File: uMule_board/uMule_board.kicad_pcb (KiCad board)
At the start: 2 copper layers, 140 x 140 mm, 212 parts, among them J1 12V IN, J10 Conn_02x04_Odd_Even, J11 Conn_01x04, J12 Conn_01x04, J13 Conn_01x04, J2 Dynamixel, J21 OUT3, J23 I2C, J26 SPI_IMU, J3 OUT3, J4 Conn_ST_STDC14, J5 OUT3, J6 OUT3, J7 ESP32_UART, J8 Li-Dar_UART, J9 Conn_02x04_Odd_Even, P1 BPV10NF, P10 BPV10NF, P11 BPV10NF, P12 BPV10NF, P13 BPV10NF, P14 BPV10NF, P15 BPV10NF, P16 BPV10NF, P2 BPV10NF, P3 BPV10NF, P4 BPV10NF, P5 BPV10NF, P6 BPV10NF, P7 BPV10NF, P8 BPV10NF, P9 BPV10NF, Q1 AON6407, Q2 AON6407, Q3 AON6407, Q4 AON6407, Q5 AON6407, SW1 DBG_BUTT, SW2 RST, U1 TPS62933DRLR, U10 OPA397DBVR, U11 OPA397DBVR, U12 OPA397DBVR, U13 OPA397DBVR, U14 OPA397DBVR, U15 OPA397DBVR, U16 OPA397DBVR, U17 OPA397DBVR, U18 OPA397DBVR, U19 OPA397DBVR, U2 TLV761, U20 OPA397DBVR, U21 OPA397DBVR, U22 OPA397DBVR, U23 SP3485CN, U24 EL3H7(B)(TA)-G, U25 EL3H7(B)(TA)-G, U26 EL3H7(B)(TA)-G, U3 INA219AxD, U4 EL3H7(B)(TA)-G, U5 STM32F103RCTx, U6 FM24C64B, U7 OPA397DBVR, U8 OPA397DBVR, U9 OPA397DBVR, Y1 8MHz

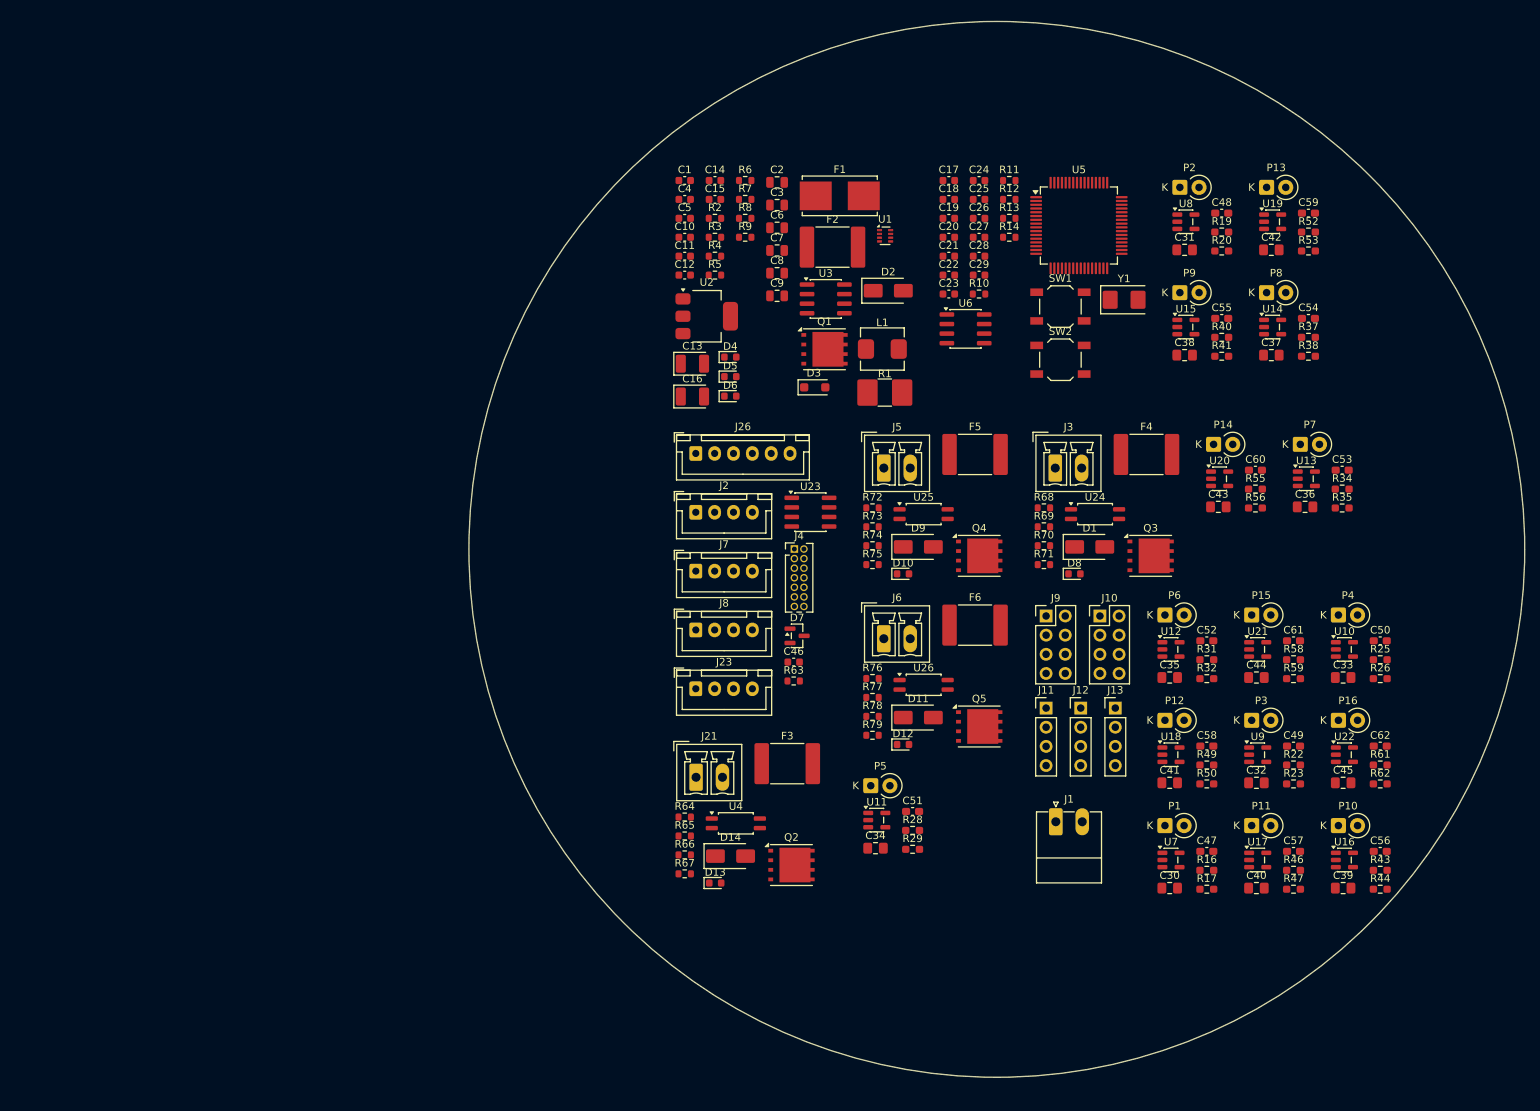
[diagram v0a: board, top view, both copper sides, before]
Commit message: Started working on PCB. Ditched high power outputs. Focusing on photodiodes. One commit closer to order
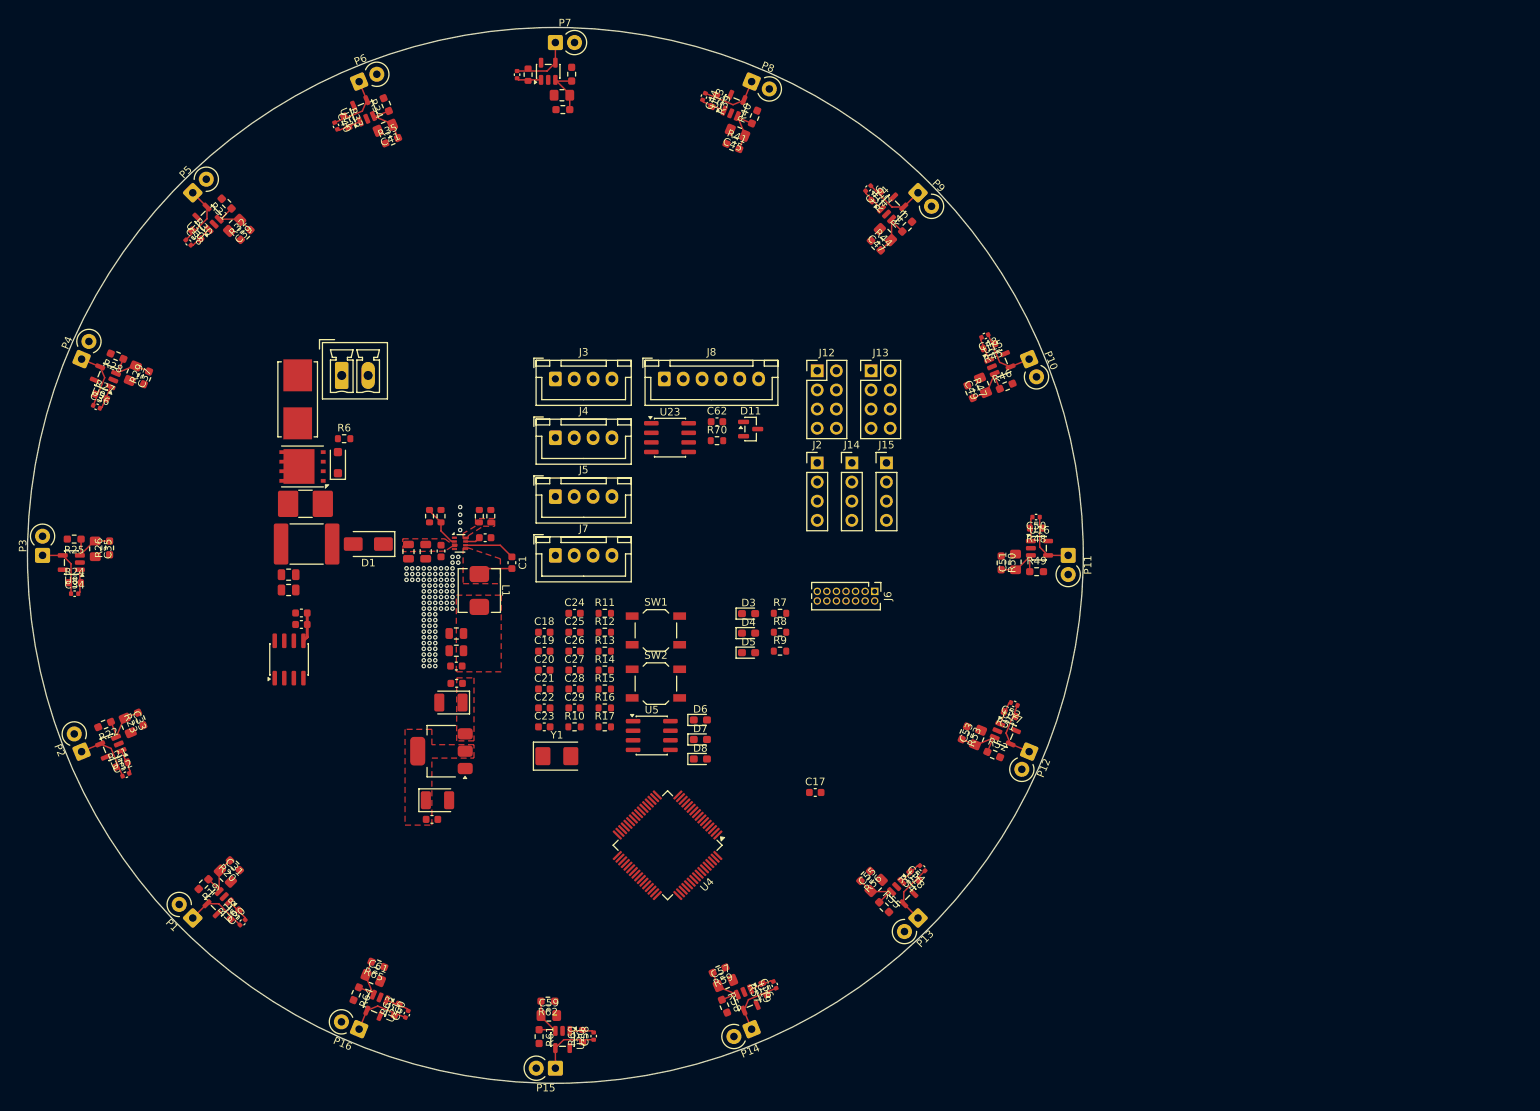
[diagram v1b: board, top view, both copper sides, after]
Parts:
- removed D10, D12, D13: OUT, LED_SMD:LED_0603_1608Metric
- removed D14, D9: SS34, Diode_SMD:D_SMA
- removed F3, F4, F5, F6: 2.5A, Fuse:Fuse_2920_7451Metric
- removed J10, J9: Conn_02x04_Odd_Even, Connector_PinHeader_2.54mm:PinHeader_2x04_P2.54mm_Vertical
- removed J11: Conn_01x04, Connector_PinHeader_2.54mm:PinHeader_1x04_P2.54mm_Vertical
- removed J21: OUT3, Connector_Phoenix_MC:PhoenixContact_MCV_1,5_2-G-3.5_1x02_P3.50mm_Vertical
- removed J23: I2C, Connector_JST:JST_XH_B4B-XH-A_1x04_P2.50mm_Vertical
- removed J26: SPI_IMU, Connector_JST:JST_XH_B6B-XH-A_1x06_P2.50mm_Vertical
- removed Q2, Q3, Q4, Q5: AON6407, Package_DFN_QFN:AO_DFN-8-1EP_5.55x5.2mm_P1.27mm_EP4.12x4.6mm
- removed R66, R74, R78: 220R, Resistor_SMD:R_0603_1608Metric
- removed R67, R71, R75, R79: 15k, Resistor_SMD:R_0603_1608Metric
- removed R68, R72, R76: 4.7k, Resistor_SMD:R_0603_1608Metric
- removed R69, R73, R77: 1k, Resistor_SMD:R_0603_1608Metric
- removed U22: OPA397DBVR, Package_TO_SOT_SMD:SOT-23-5
- removed U24, U25, U26: EL3H7(B)(TA)-G, Package_SO:SOP-4_4.4x2.6mm_P1.27mm
- added J14: Conn_01x04, Connector_PinHeader_2.54mm:PinHeader_1x04_P2.54mm_Vertical, F.Cu at (127.8, 82.5)
- added J15: Conn_01x04, Connector_PinHeader_2.54mm:PinHeader_1x04_P2.54mm_Vertical, F.Cu at (132.4, 82.5)
- added R15: 2.2k, Resistor_SMD:R_0603_1608Metric, F.Cu at (95.0, 112.5)
- added R18: 39k, Resistor_SMD:R_0603_1608Metric, F.Cu at (45.9, 142.4)
- added R21: 39k, Resistor_SMD:R_0603_1608Metric, F.Cu at (31.0, 122.5)
- added R24: 39k, Resistor_SMD:R_0603_1608Metric, F.Cu at (24.7, 98.4)
- added R27: 39k, Resistor_SMD:R_0603_1608Metric, F.Cu at (28.2, 73.7)
- added R30: 39k, Resistor_SMD:R_0603_1608Metric, F.Cu at (40.8, 52.3)
- added R33: 39k, Resistor_SMD:R_0603_1608Metric, F.Cu at (60.7, 37.3)
- added R36: 39k, Resistor_SMD:R_0603_1608Metric, F.Cu at (84.8, 31.1)
- added R39: 39k, Resistor_SMD:R_0603_1608Metric, F.Cu at (109.5, 34.5)
- added R42: 39k, Resistor_SMD:R_0603_1608Metric, F.Cu at (131.0, 47.2)
- added R45: 39k, Resistor_SMD:R_0603_1608Metric, F.Cu at (146.0, 67.1)
- added R48: 39k, Resistor_SMD:R_0603_1608Metric, F.Cu at (152.2, 91.2)
- added R51: 39k, Resistor_SMD:R_0603_1608Metric, F.Cu at (148.7, 115.8)
- added R54: 39k, Resistor_SMD:R_0603_1608Metric, F.Cu at (136.1, 137.3)
- added R57: 39k, Resistor_SMD:R_0603_1608Metric, F.Cu at (116.2, 152.3)
- added R60: 39k, Resistor_SMD:R_0603_1608Metric, F.Cu at (92.1, 158.5)
- C30, C32, C34, C36, C38, C40, C42, C44: value 1u -> 2.7p; footprint Capacitor_SMD:C_0805_2012Metric_Pad1.18x1.45mm_HandSolder -> Capacitor_SMD:C_0402_1005Metric
- C46: value 100n -> 2.7p; footprint Capacitor_SMD:C_0603_1608Metric -> Capacitor_SMD:C_0402_1005Metric
- C47, C49, C51, C53, C55, C57, C59, C61: value 2.7p -> 1u; footprint Capacitor_SMD:C_0603_1608Metric_Pad1.08x0.95mm_HandSolder -> Capacitor_SMD:C_0805_2012Metric_Pad1.18x1.45mm_HandSolder
- C48, C50, C52, C54, C56, C58, C60: footprint Capacitor_SMD:C_0603_1608Metric_Pad1.08x0.95mm_HandSolder -> Capacitor_SMD:C_0402_1005Metric
- C62: value 2.7p -> 100n; footprint Capacitor_SMD:C_0603_1608Metric_Pad1.08x0.95mm_HandSolder -> Capacitor_SMD:C_0603_1608Metric
- D11: value SS34 -> SM712_SOT23; footprint Diode_SMD:D_SMA -> Package_TO_SOT_SMD:SOT-23
- D2: value SS34 -> BZT52B12; footprint Diode_SMD:D_SMA -> Diode_SMD:D_SOD-123F
- D3: value BZT52B12 -> LED; footprint Diode_SMD:D_SOD-123F -> LED_SMD:LED_0603_1608Metric_Pad1.05x0.95mm_HandSolder
- D4, D5: value LED_RED -> LED; footprint LED_SMD:LED_0603_1608Metric -> LED_SMD:LED_0603_1608Metric_Pad1.05x0.95mm_HandSolder
- D6: value LED_RED -> RED; footprint LED_SMD:LED_0603_1608Metric -> LED_SMD:LED_0603_1608Metric_Pad1.05x0.95mm_HandSolder
- D7: value SM712_SOT23 -> BLUE; footprint Package_TO_SOT_SMD:SOT-23 -> LED_SMD:LED_0603_1608Metric_Pad1.05x0.95mm_HandSolder
- D8: value OUT -> BLUE; footprint LED_SMD:LED_0603_1608Metric -> LED_SMD:LED_0603_1608Metric_Pad1.05x0.95mm_HandSolder
- J1: footprint Connector_Phoenix_MC:PhoenixContact_MC_1,5_2-G-3.5_1x02_P3.50mm_Horizontal -> Connector_Phoenix_MC:PhoenixContact_MCV_1,5_2-G-3.5_1x02_P3.50mm_Vertical
- J12, J13: value Conn_01x04 -> Conn_02x04_Odd_Even; footprint Connector_PinHeader_2.54mm:PinHeader_1x04_P2.54mm_Vertical -> Connector_PinHeader_2.54mm:PinHeader_2x04_P2.54mm_Vertical
- J2: value Dynamixel -> Conn_01x04; footprint Connector_JST:JST_XH_B4B-XH-A_1x04_P2.50mm_Vertical -> Connector_PinHeader_2.54mm:PinHeader_1x04_P2.54mm_Vertical
- J3: value OUT3 -> Dynamixel; footprint Connector_Phoenix_MC:PhoenixContact_MCV_1,5_2-G-3.5_1x02_P3.50mm_Vertical -> Connector_JST:JST_XH_B4B-XH-A_1x04_P2.50mm_Vertical
- J4: value Conn_ST_STDC14 -> Li-Dar_UART; footprint Connector_PinHeader_1.27mm:PinHeader_2x07_P1.27mm_Vertical -> Connector_JST:JST_XH_B4B-XH-A_1x04_P2.50mm_Vertical
- J5: value OUT3 -> ESP32_UART; footprint Connector_Phoenix_MC:PhoenixContact_MCV_1,5_2-G-3.5_1x02_P3.50mm_Vertical -> Connector_JST:JST_XH_B4B-XH-A_1x04_P2.50mm_Vertical
- J6: value OUT3 -> Conn_ST_STDC14; footprint Connector_Phoenix_MC:PhoenixContact_MCV_1,5_2-G-3.5_1x02_P3.50mm_Vertical -> Connector_PinHeader_1.27mm:PinHeader_2x07_P1.27mm_Vertical
- J7: value ESP32_UART -> I2C
- J8: value Li-Dar_UART -> SPI_IMU; footprint Connector_JST:JST_XH_B4B-XH-A_1x04_P2.50mm_Vertical -> Connector_JST:JST_XH_B6B-XH-A_1x06_P2.50mm_Vertical
- R16: value 13.7 -> 1.5k; footprint Resistor_SMD:R_0603_1608Metric_Pad0.98x0.95mm_HandSolder -> Resistor_SMD:R_0603_1608Metric
- R17: value 280 -> 1.5k; footprint Resistor_SMD:R_0603_1608Metric_Pad0.98x0.95mm_HandSolder -> Resistor_SMD:R_0603_1608Metric
- R4: value 10k -> 120k
- R5: value 120k -> 6.2k
- R6: value 6.2k -> 10k
- R63: value 120R -> 39k
- R64: value 4.7k -> 13.7; footprint Resistor_SMD:R_0603_1608Metric -> Resistor_SMD:R_0603_1608Metric_Pad0.98x0.95mm_HandSolder
- R65: value 1k -> 280; footprint Resistor_SMD:R_0603_1608Metric -> Resistor_SMD:R_0603_1608Metric_Pad0.98x0.95mm_HandSolder
- R7: value 15k -> 14k
- R70: value 220R -> 120R
- U1: value TPS62933DRLR -> TPS62933
- U4: value EL3H7(B)(TA)-G -> STM32F103RCTx; footprint Package_SO:SOP-4_4.4x2.6mm_P1.27mm -> Package_QFP:LQFP-64_10x10mm_P0.5mm
- U5: value STM32F103RCTx -> FM24C64B; footprint Package_QFP:LQFP-64_10x10mm_P0.5mm -> Package_SO:SOIC-8_3.9x4.9mm_P1.27mm
- U6: value FM24C64B -> OPA397DBVR; footprint Package_SO:SOIC-8_3.9x4.9mm_P1.27mm -> Package_TO_SOT_SMD:SOT-23-5
- moved R25 173.9 mm to (24.7, 92.6), turned to 180 degrees
- moved C39 171.3 mm to (45.9, 51.0), turned to -135 degrees
- moved P4 170.1 mm to (25.6, 68.8), turned to 67.5 degrees
- moved R26 169.4 mm to (29.4, 93.8), turned to 90 degrees
- moved P2 163.7 mm to (25.6, 120.8), turned to 112.5 degrees
- moved P3 161.8 mm to (20.5, 94.8), turned to 90 degrees
- moved C33 161.3 mm to (31.8, 117.3), turned to -67.5 degrees
- moved U10 161.2 mm to (42.4, 50.1), turned to 135 degrees
- moved U9 160.8 mm to (28.8, 71.1), turned to 157.5 degrees
- moved C36 160.8 mm to (27.6, 75.1), turned to -22.5 degrees
- moved R19 160.3 mm to (41.8, 138.4), turned to -135 degrees
- moved C40 158.5 mm to (59.4, 37.9), turned to -67.5 degrees
- moved R22 157.7 mm to (28.7, 117.2), turned to -157.5 degrees
- moved U8 154.6 mm to (24.3, 95.7), turned to 180 degrees
- moved R20 154.1 mm to (46.0, 135.9), turned to 135 degrees
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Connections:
- C25 pad 1: Net-(U5-PD0) -> Net-(U4-PD0)
- C26 pad 1: Net-(U5-PD1) -> Net-(U4-PD1)
- C30 pad 1: Net-(U7-+) -> Net-(P1-K)
- C30 pad 2: GND -> /PHO_0
- C31 pad 1: Net-(U8-+) -> Net-(U6-+)
- C32 pad 1: Net-(U9-+) -> Net-(P2-K)
- C32 pad 2: GND -> /PHO_1
- C33 pad 1: Net-(U10-+) -> Net-(U7-+)
- C34 pad 1: Net-(U11-+) -> Net-(P3-K)
- C34 pad 2: GND -> /PHO_2
- C35 pad 1: Net-(U12-+) -> Net-(U8-+)
- C36 pad 1: Net-(U13-+) -> Net-(P4-K)
- C36 pad 2: GND -> /PHO_3
- C37 pad 1: Net-(U14-+) -> Net-(U9-+)
- C38 pad 1: Net-(U15-+) -> Net-(P5-K)
- C38 pad 2: GND -> /PHO_4
- C39 pad 1: Net-(U16-+) -> Net-(U10-+)
- C40 pad 1: Net-(U17-+) -> Net-(P6-K)
- C40 pad 2: GND -> /PHO_5
- C41 pad 1: Net-(U18-+) -> Net-(U11-+)
- C42 pad 1: Net-(U19-+) -> Net-(P7-K)
- C42 pad 2: GND -> /PHO_6
- C43 pad 1: Net-(U20-+) -> Net-(U12-+)
- C44 pad 1: Net-(U21-+) -> Net-(P8-K)
- C44 pad 2: GND -> /PHO_7
- C45 pad 1: Net-(U22-+) -> Net-(U13-+)
- C46 pad 1: GND -> Net-(P9-K)
- C46 pad 2: +3V3 -> /PHO_8
- C47 pad 1: Net-(P1-K) -> Net-(U14-+)
- C47 pad 2: /PHO_0 -> GND
- C48 pad 1: Net-(P2-K) -> Net-(P10-K)
- C48 pad 2: /PHO_1 -> /PHO_9
- C49 pad 1: Net-(P3-K) -> Net-(U15-+)
- C49 pad 2: /PHO_2 -> GND
- C50 pad 1: Net-(P4-K) -> Net-(P11-K)
- C50 pad 2: /PHO_3 -> /PHO_10
- C51 pad 1: Net-(P5-K) -> Net-(U16-+)
- C51 pad 2: /PHO_4 -> GND
- C52 pad 1: Net-(P6-K) -> Net-(P12-K)
- C52 pad 2: /PHO_5 -> /PHO_11
- C53 pad 1: Net-(P7-K) -> Net-(U17-+)
- C53 pad 2: /PHO_6 -> GND
- C54 pad 1: Net-(P8-K) -> Net-(P13-K)
- C54 pad 2: /PHO_7 -> /PHO_12
- C55 pad 1: Net-(P9-K) -> Net-(U18-+)
- C55 pad 2: /PHO_8 -> GND
- C56 pad 1: Net-(P10-K) -> Net-(P14-K)
- C56 pad 2: /PHO_9 -> /PHO_13
- C57 pad 1: Net-(P11-K) -> Net-(U19-+)
- C57 pad 2: /PHO_10 -> GND
- C58 pad 1: Net-(P12-K) -> Net-(P15-K)
- C58 pad 2: /PHO_11 -> /PHO_14
- C59 pad 1: Net-(P13-K) -> Net-(U20-+)
- C59 pad 2: /PHO_12 -> GND
- C60 pad 1: Net-(P14-K) -> Net-(P16-K)
- C60 pad 2: /PHO_13 -> /PHO_15
- C61 pad 1: Net-(P15-K) -> Net-(U21-+)
- C61 pad 2: /PHO_14 -> GND
- C62 pad 1: Net-(P16-K) -> GND
- C62 pad 2: /PHO_15 -> +3V3
- D1 pad 1: Net-(D1-K) -> /Power/DC_CONV_IN
- D1 pad 2: GND -> Net-(D1-A)
- D11 pad 1: Net-(D11-K) -> /Communication/RS485-
- D11 pad 2: GND -> /Communication/RS485+
- D2 pad 1: /Power/DC_CONV_IN -> /Power/R_SHUNT_+
- D3 pad 1: /Power/R_SHUNT_+ -> GND
- D7 pad 1: /Communication/A -> GND
- D7 pad 2: /Communication/B -> Net-(D7-A)
- F2 pad 2: Net-(D2-A) -> Net-(D1-A)
- J12 pad 1: /GPIO/GPIO_4 -> +3V3
- J12 pad 2: /GPIO/GPIO_5 -> GND
- J12 pad 3: /GPIO/GPIO_6 -> +3V3
- J12 pad 4: /GPIO/GPIO_7 -> GND
- J13 pad 1: /GPIO/GPIO_8 -> +5V
- J13 pad 2: /GPIO/GPIO_9 -> GND
- J13 pad 3: /GPIO/GPIO_10 -> +5V
- J13 pad 4: unconnected-(J13-Pin_4-Pad4) -> GND
- J2 pad 1: VCC -> /GPIO/GPIO_8
- J2 pad 2: /Communication/A -> /GPIO/GPIO_9
- J2 pad 3: /Communication/B -> /GPIO/GPIO_10
- J2 pad 4: GND -> /GPIO/GPIO_11
- J3 pad 1: Net-(D1-K) -> VCC
- J3 pad 2: GND -> /Communication/RS485-
- J4 pad 1: unconnected-(J4-NC-Pad1) -> +5V
- J4 pad 2: unconnected-(J4-NC-Pad2) -> /Communication/Li-Dar_TX
- J4 pad 3: +3V3 -> /Communication/Li-Dar_RX
- J4 pad 4: /Communication/SWDIO -> GND
- J5 pad 1: Net-(D9-K) -> +5V
- J5 pad 2: GND -> /Communication/ESP32_TX
- J6 pad 1: Net-(D11-K) -> unconnected-(J6-NC-Pad1)
- J6 pad 2: GND -> unconnected-(J6-NC-Pad2)
- J7 pad 1: +5V -> +3V3
- J7 pad 2: /Communication/ESP32_TX -> /MCU/I2C1_SCL
- J7 pad 3: /Communication/ESP32_RX -> /MCU/I2C1_SDA
- J8 pad 1: +5V -> +3V3
- J8 pad 2: /Communication/Li-Dar_TX -> /Communication/SPI_SCK
- J8 pad 3: /Communication/Li-Dar_RX -> /Communication/SPI_MISO
- J8 pad 4: GND -> /Communication/SPI_MOSI
- Q1 pad 4: Net-(D3-A) -> Net-(D2-A)
- R16 pad 1: Net-(U7-+) -> /MCU/DBG_LED1
- R16 pad 2: +5V -> Net-(D7-A)
- R17 pad 1: GND -> /MCU/DBG_LED0
- R17 pad 2: Net-(U7-+) -> Net-(D8-A)
- R19 pad 1: Net-(U8-+) -> Net-(U6-+)
- R20 pad 2: Net-(U8-+) -> Net-(U6-+)
- R22 pad 1: Net-(U9-+) -> Net-(U7-+)
- R23 pad 2: Net-(U9-+) -> Net-(U7-+)
- R25 pad 1: Net-(U10-+) -> Net-(U8-+)
- R26 pad 2: Net-(U10-+) -> Net-(U8-+)
- R28 pad 1: Net-(U11-+) -> Net-(U9-+)
- R29 pad 2: Net-(U11-+) -> Net-(U9-+)
- R31 pad 1: Net-(U12-+) -> Net-(U10-+)
- R32 pad 2: Net-(U12-+) -> Net-(U10-+)
- R34 pad 1: Net-(U13-+) -> Net-(U11-+)
- R35 pad 2: Net-(U13-+) -> Net-(U11-+)
- R37 pad 1: Net-(U14-+) -> Net-(U12-+)
- R38 pad 2: Net-(U14-+) -> Net-(U12-+)
- R4 pad 1: Net-(D3-A) -> Net-(U1-EN)
- R40 pad 1: Net-(U15-+) -> Net-(U13-+)
- R41 pad 2: Net-(U15-+) -> Net-(U13-+)
- R43 pad 1: Net-(U16-+) -> Net-(U14-+)
- R44 pad 2: Net-(U16-+) -> Net-(U14-+)
- R46 pad 1: Net-(U17-+) -> Net-(U15-+)
- R47 pad 2: Net-(U17-+) -> Net-(U15-+)
- R49 pad 1: Net-(U18-+) -> Net-(U16-+)
- R5 pad 1: Net-(U1-EN) -> Net-(U1-FB)
- R50 pad 2: Net-(U18-+) -> Net-(U16-+)
- R52 pad 1: Net-(U19-+) -> Net-(U17-+)
- R53 pad 2: Net-(U19-+) -> Net-(U17-+)
- R55 pad 1: Net-(U20-+) -> Net-(U18-+)
- R56 pad 2: Net-(U20-+) -> Net-(U18-+)
- R58 pad 1: Net-(U21-+) -> Net-(U19-+)
- R59 pad 2: Net-(U21-+) -> Net-(U19-+)
- R6 pad 1: Net-(U1-FB) -> Net-(D2-A)
- R61 pad 1: Net-(U22-+) -> Net-(U20-+)
- R62 pad 2: Net-(U22-+) -> Net-(U20-+)
- R63 pad 1: /Communication/B -> Net-(P16-K)
- R63 pad 2: /Communication/A -> /PHO_15
- R64 pad 1: VCC -> Net-(U21-+)
- R64 pad 2: Net-(Q2-G) -> +5V
- R65 pad 1: Net-(Q2-G) -> GND
- R65 pad 2: Net-(R65-Pad2) -> Net-(U21-+)
- R7 pad 2: Net-(D4-A) -> Net-(D3-A)
- R70 pad 1: Net-(R70-Pad1) -> /Communication/RS485+
- R70 pad 2: /MCU/PC7/OUT1 -> /Communication/RS485-
- R8 pad 2: Net-(D5-A) -> Net-(D4-A)
- R9 pad 2: Net-(D6-A) -> Net-(D5-A)
- U10 pad 1: /PHO_3 -> /PHO_4
- U10 pad 4: Net-(P4-K) -> Net-(P5-K)
- U11 pad 1: /PHO_4 -> /PHO_5
- U11 pad 4: Net-(P5-K) -> Net-(P6-K)
- U12 pad 1: /PHO_5 -> /PHO_6
- U12 pad 4: Net-(P6-K) -> Net-(P7-K)
- U13 pad 1: /PHO_6 -> /PHO_7
- U13 pad 4: Net-(P7-K) -> Net-(P8-K)
- U14 pad 1: /PHO_7 -> /PHO_8
- U14 pad 4: Net-(P8-K) -> Net-(P9-K)
- U15 pad 1: /PHO_8 -> /PHO_9
- U15 pad 4: Net-(P9-K) -> Net-(P10-K)
- U16 pad 1: /PHO_9 -> /PHO_10
- U16 pad 4: Net-(P10-K) -> Net-(P11-K)
- U17 pad 1: /PHO_10 -> /PHO_11
- U17 pad 4: Net-(P11-K) -> Net-(P12-K)
- U18 pad 1: /PHO_11 -> /PHO_12
- U18 pad 4: Net-(P12-K) -> Net-(P13-K)
- U19 pad 1: /PHO_12 -> /PHO_13
- U19 pad 4: Net-(P13-K) -> Net-(P14-K)
- U20 pad 1: /PHO_13 -> /PHO_14
- U20 pad 4: Net-(P14-K) -> Net-(P15-K)
- U21 pad 1: /PHO_14 -> /PHO_15
- U21 pad 4: Net-(P15-K) -> Net-(P16-K)
- U23 pad 6: /Communication/A -> /Communication/RS485-
- U23 pad 7: /Communication/B -> /Communication/RS485+
- U4 pad 1: Net-(R66-Pad1) -> +3V3
- U4 pad 2: GND -> /GPIO/GPIO_5
- U4 pad 3: GND -> /GPIO/GPIO_6
- U4 pad 4: Net-(R65-Pad2) -> /GPIO/GPIO_7
- U5 pad 1: +3V3 -> GND
- U5 pad 2: /GPIO/GPIO_8 -> GND
- U5 pad 3: /GPIO/GPIO_9 -> GND
- U5 pad 4: /GPIO/GPIO_10 -> GND
- U5 pad 5: Net-(U5-PD0) -> /MCU/I2C1_SDA
- U5 pad 6: Net-(U5-PD1) -> /MCU/I2C1_SCL
- U5 pad 7: /MCU/NRST -> GND
- U5 pad 8: /PHO_10 -> +3V3
- U6 pad 1: GND -> /PHO_0
- U6 pad 3: GND -> Net-(U6-+)
- U6 pad 4: GND -> Net-(P1-K)
- U6 pad 5: /MCU/I2C1_SDA -> +5V
- U7 pad 1: /PHO_0 -> /PHO_1
- U7 pad 4: Net-(P1-K) -> Net-(P2-K)
- U8 pad 1: /PHO_1 -> /PHO_2
- U8 pad 4: Net-(P2-K) -> Net-(P3-K)
- U9 pad 1: /PHO_2 -> /PHO_3
- U9 pad 4: Net-(P3-K) -> Net-(P4-K)
- Y1 pad 1: Net-(U5-PD1) -> Net-(U4-PD1)
- Y1 pad 2: Net-(U5-PD0) -> Net-(U4-PD0)
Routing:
- net Net-(P16-K): track 0.00 -> 8.21 mm
- net Net-(P8-K): track 0.00 -> 8.21 mm
- net Net-(P12-K): track 0.00 -> 8.21 mm
- net Net-(P4-K): track 0.00 -> 8.21 mm
- net Net-(P1-K): track 0.00 -> 8.21 mm
- net Net-(P9-K): track 0.00 -> 8.21 mm
- net Net-(P5-K): track 0.00 -> 8.21 mm
- net Net-(P13-K): track 0.00 -> 8.21 mm
- net Net-(P11-K): track 0.00 -> 8.21 mm
- net Net-(P7-K): track 0.00 -> 8.21 mm
- net Net-(P3-K): track 0.00 -> 8.21 mm
- net Net-(P15-K): track 0.00 -> 8.21 mm
- net Net-(P14-K): track 0.00 -> 8.21 mm
- net Net-(P6-K): track 0.00 -> 8.21 mm
- net Net-(P10-K): track 0.00 -> 8.21 mm
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- added copper zone on F.Cu, net +3V3
- added copper zone on F.Cu, net +5V
- added copper zone on F.Cu, net /Power/DC_CONV_IN
- added copper zone on F.Cu, net Net-(U1-FB)
- added copper zone on F.Cu, net Net-(U1-SW)
